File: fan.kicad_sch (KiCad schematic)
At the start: 16 parts, among them J6 Conn_01x04, J7 Conn_01x04, Q3 MMBT3906, U10 EMC2101

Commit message: All components placed
Went through TI schematic and layout checklist.
All components placed and initial DRC
Need thermal vias on KF1950 and also better layout (so not so many errors)
Need to do silk
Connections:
- no-connect marks 0 -> 1
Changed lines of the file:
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@@
 		(color 0 0 0 0)
+	)
+	(no_connect
+		(at 193.04 104.14)
 	)
 	(wire

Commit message: Silk Done
Still need to fix up heatsink vias on ASIC and paste layer for thermal
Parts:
- renumbered TP38 to FANPWM, TP37 to FANTACH
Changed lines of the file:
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@@
 		(on_board yes)
 		(dnp no)
-		(property "Reference" "TP38"
-			(at 162.56 109.22 90)
+		(property "Reference" "FANPWM"
+			(at 160.02 109.22 90)
 			(effects
 				(font
@@
 			(project "bitaxeGamma"
 				(path "/e63e39d7-6ac0-4ffd-8aa3-1841a4541b55/8e8832ea-6bf1-49d2-b3a5-32a207f555d2"
-					(reference "TP38")
+					(reference "FANPWM")
 					(unit 1)
 				)
@@
 		(on_board yes)
 		(dnp no)
-		(property "Reference" "TP37"
-			(at 129.54 111.76 90)
+		(property "Reference" "FANTACH"
+			(at 127 111.76 90)
 			(effects
 				(font
@@
 			(project "bitaxeGamma"
 				(path "/e63e39d7-6ac0-4ffd-8aa3-1841a4541b55/8e8832ea-6bf1-49d2-b3a5-32a207f555d2"
-					(reference "TP37")
-					(unit 1)
-				)
+					(reference "FANTACH")
+					(unit 1)
+				)

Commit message: Manfacturing prep
Add part numbers and did initial BOM optimization (Hope to do more after testing)
Created Manufacturing files
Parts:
- renumbered FANPWM to FANPWM1, FANTACH to FANTACH1, TP36 to TEMP_N1, TP35 to TEMP_P1
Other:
- note added: "This sets default fan speed to 100% -> 5.6k is datasheet recommendation but would be nice to use 4.64k"
- note removed: "This sets default fan speed to 100% ->"
- moved on the sheet: Q3, R22, R23, TEMP_N1, TEMP_P1

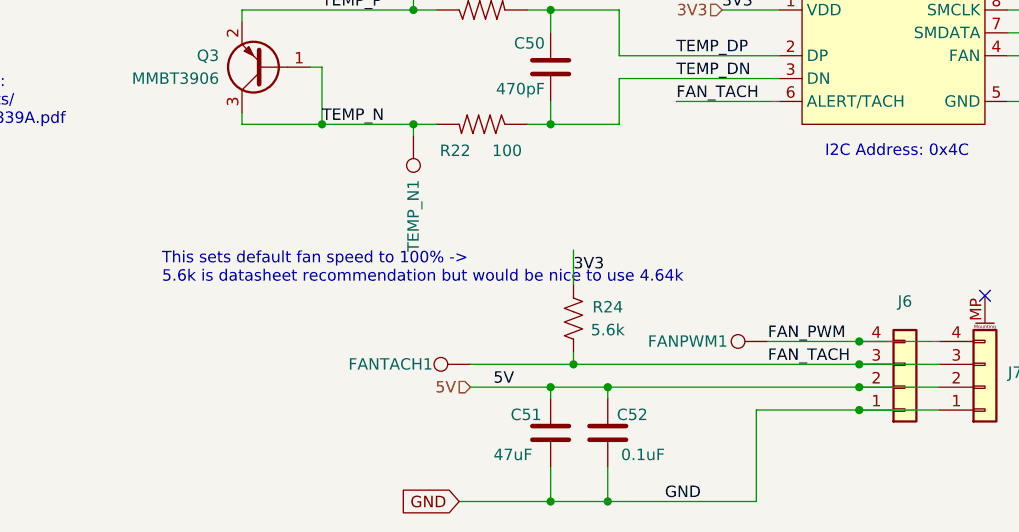
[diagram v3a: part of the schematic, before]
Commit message: Addressed Bitaxe Gamma Issues
- moved Fan caps
- added USB CC1 & CC2 pulldowns
- (I2C pullups were already done)
- reviewed but so far did not address any of the other issues/bugs
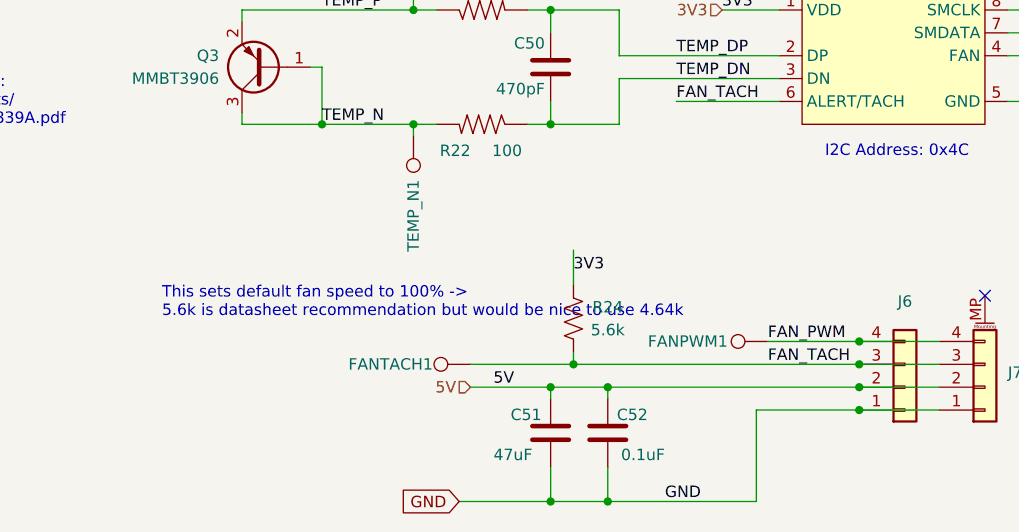
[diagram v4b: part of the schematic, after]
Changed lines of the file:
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@@
 	(text "This sets default fan speed to 100% ->\n5.6k is datasheet recommendation but would be nice to use 4.64k"
 		(exclude_from_sim no)
-		(at 101.6 102.87 0)
+		(at 101.6 106.68 0)
 		(effects
 			(font
